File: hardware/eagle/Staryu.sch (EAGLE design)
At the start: 29 parts, among them IC1 ATMEGA32U2-TQFP, SW1 CHERRY-MX-LED, SW2 CHERRY-MX-LED, SW3 CHERRY-MX-LED, SW4 CHERRY-MX-LED, SW5 CHERRY-MX-LED, Y1 16MHZ

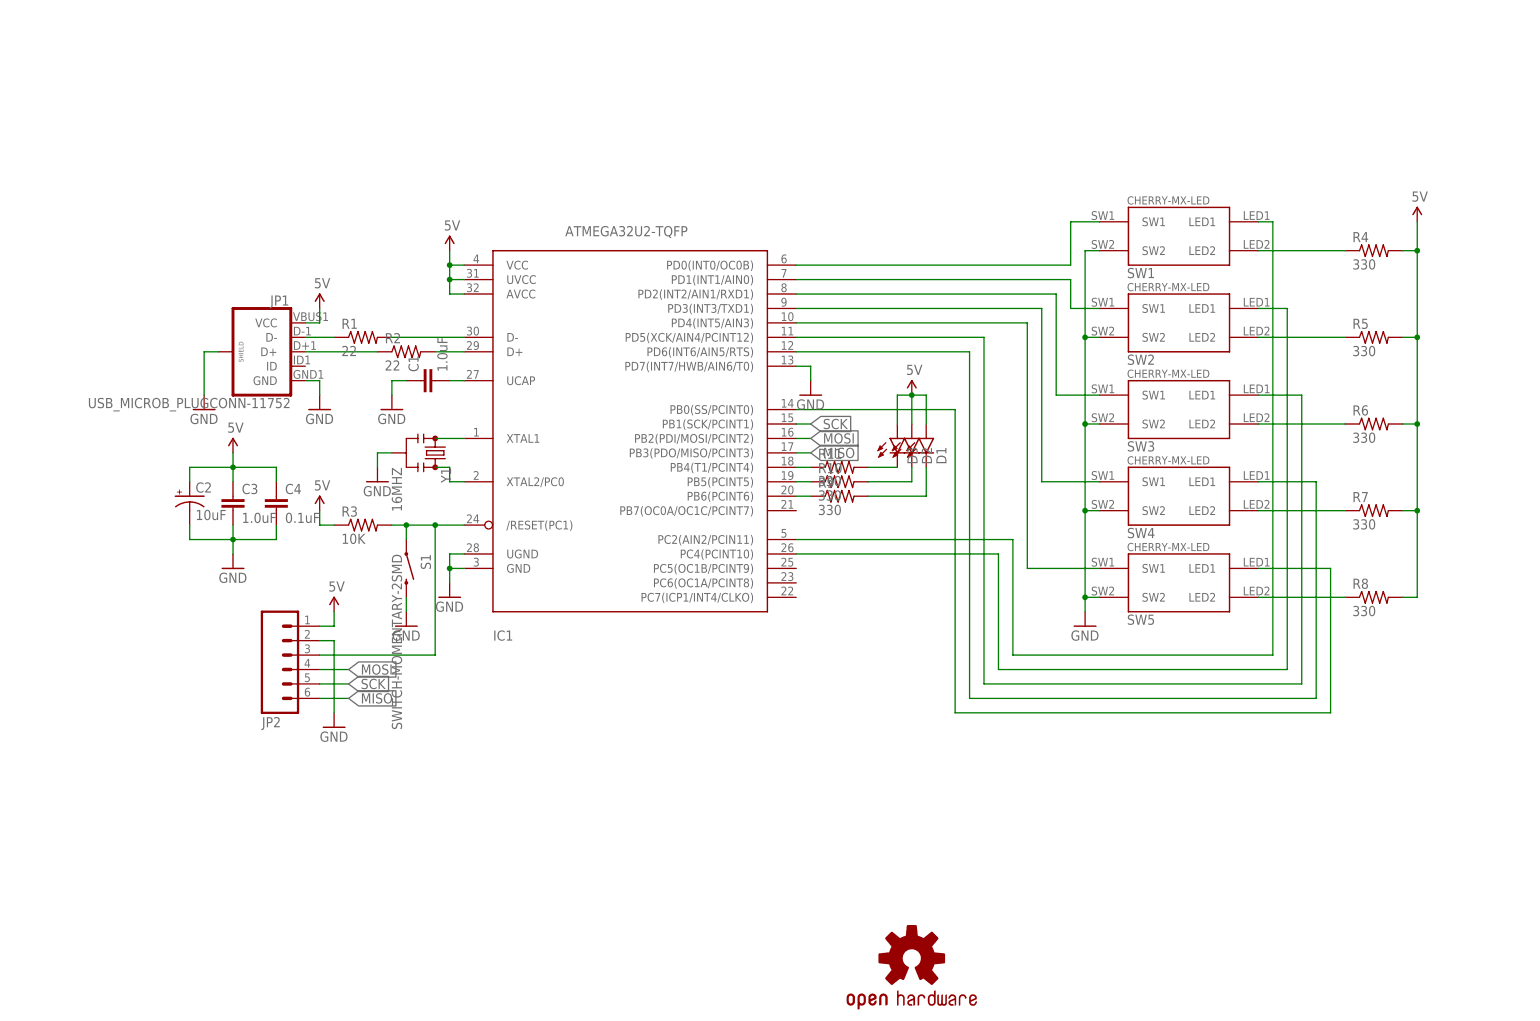
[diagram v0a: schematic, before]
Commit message: Update eagle files and schematics to v1.2 - Change 3 LEDs on top side to WS2812B
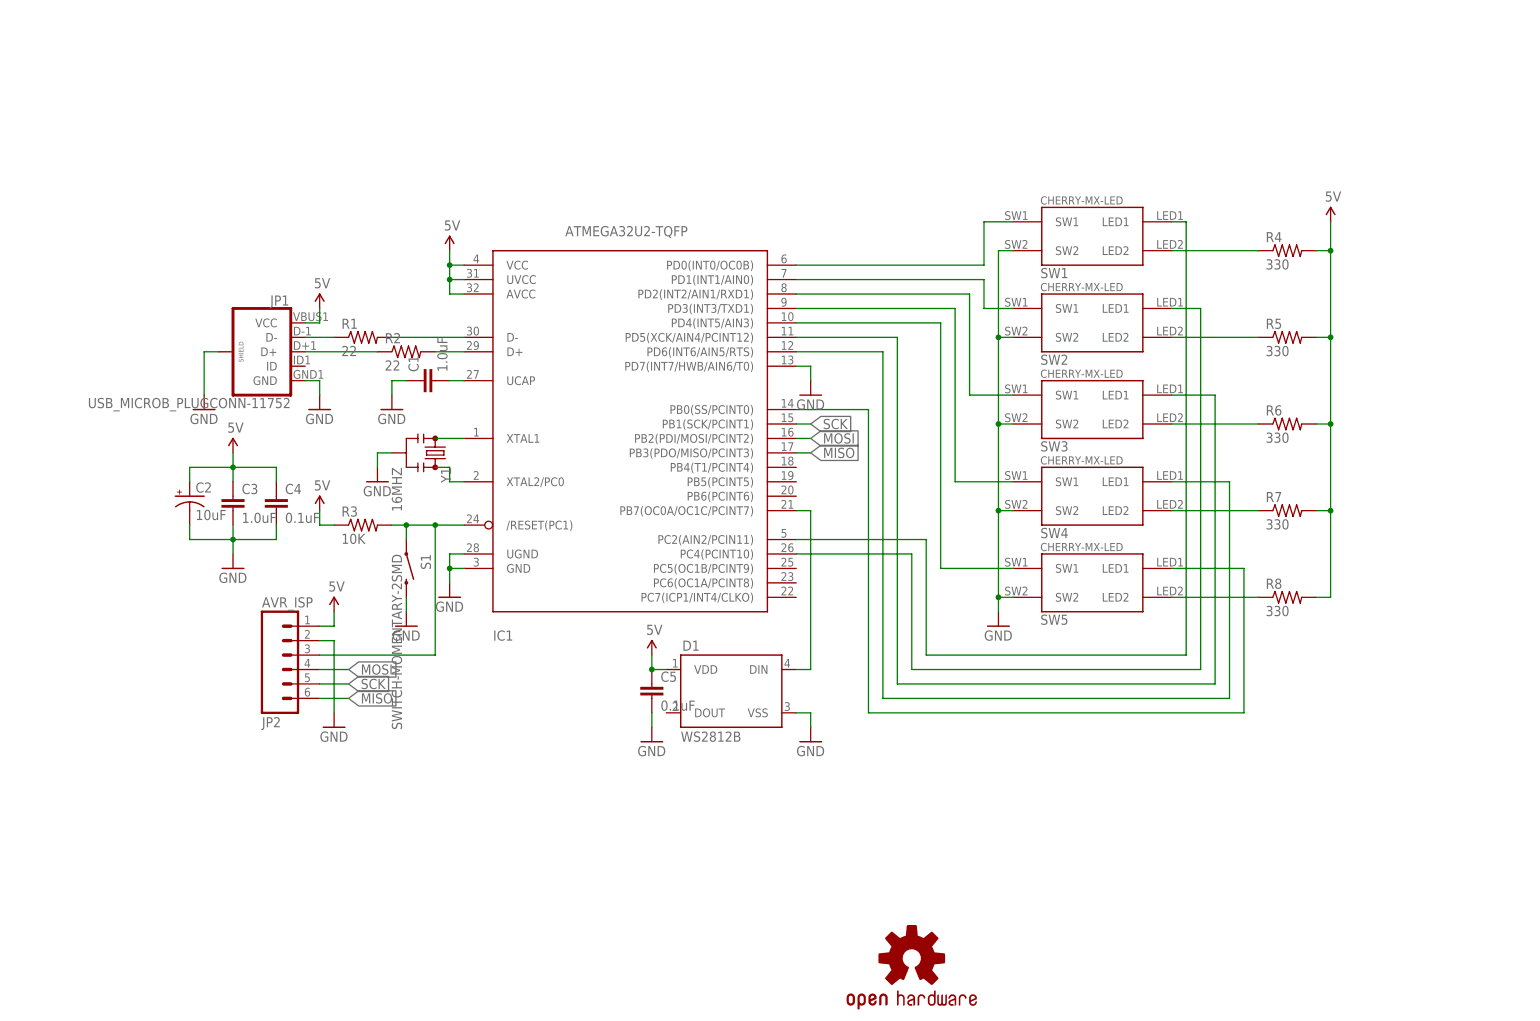
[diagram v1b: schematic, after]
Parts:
- removed D2, D3: (no value), SparkFun-LED:LED1206
- removed R10, R11, R9: 330, SparkFun-Resistors:330OHM1/10W1%(0603)
- added C5: 0.1uF, SparkFun-Capacitors:0.1UF-25V(+80/-20%)(0603)
- D1: value (none) -> WS2812B; device SparkFun-LED:LED1206 -> SparkFun-LED:WS2812B
- JP2: value (none) -> AVR_ISP
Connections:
- removed net N$20: IC1.PB5(PCINT5), R10.1
- removed net N$21: IC1.PB6(PCINT6), R9.1
- removed net N$27: D3.C, R11.2
- removed net N$28: D2.C, R10.2
- removed net N$29: D1.C, R9.2
- net 5V: now also C5.1, D1.VDD; no longer D1.A, D2.A, D3.A
- net GND: now also C5.2, D1.VSS
- net N$19: now also D1.DIN, IC1.PB7(OC0A/OC1C/PCINT7); no longer IC1.PB4(T1/PCINT4), R11.1
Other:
- moved on the sheet: R4, R5, R6, R7, R8, SW1, SW2, SW3, SW4, SW5

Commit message: Update eagle files and schematics to v1.2 - Compact outline - Relocate LED and re-route circuits - Add logos
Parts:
- added LOGO2: NOUKENSHA-LOGOM, Noukensha:NOUKENSHA-LOGOM
- added LOGO3: OSHW-LOGOM, Noukensha:OSHW-LOGOM
- added U$3: CC-BY-SANIX, cc-by-sa:CC-BY-SANIX
- C1, C3: device SparkFun-Capacitors:1.0UF-16V-10%(0603) -> SparkFun-Capacitors:CAP0805
- C4, C5: device SparkFun-Capacitors:0.1UF-25V(+80/-20%)(0603) -> SparkFun-Capacitors:CAP0805
- D1: device SparkFun-LED:WS2812B -> ws2812:WS2812BNOSILK
- LOGO1: value OSHW-LOGOM -> STARYU-LOGO; device SparkFun-Aesthetics:OSHW-LOGOM -> Noukensha:STARYU-LOGO
- R1, R2: device SparkFun-Resistors:22OHM1/10W1%(0603) -> SparkFun-Resistors:RESISTOR0805-RES
- R3: device SparkFun-Resistors:10KOHM-1/10W-1%(0603)0603 -> SparkFun-Resistors:RESISTOR0805-RES
- R4, R5, R6, R7, R8: device SparkFun-Resistors:330OHM1/10W1%(0603) -> SparkFun-Resistors:RESISTOR0805-RES
- renumbered IC1 to U1
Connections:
- new net SHIELD: JP1.SHIELD
- net GND: now also S1.1; no longer JP1.SHIELD, S1.2
- net N$19: now also U1.PC6(OC1A/PCINT8); no longer U1.PB7(OC0A/OC1C/PCINT7)
- net N$31: now also U1.PC7(ICP1/INT4/CLKO); no longer U1.PC4(PCINT10)
- net N$8: now also S1.2; no longer S1.1
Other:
- moved on the sheet: S1

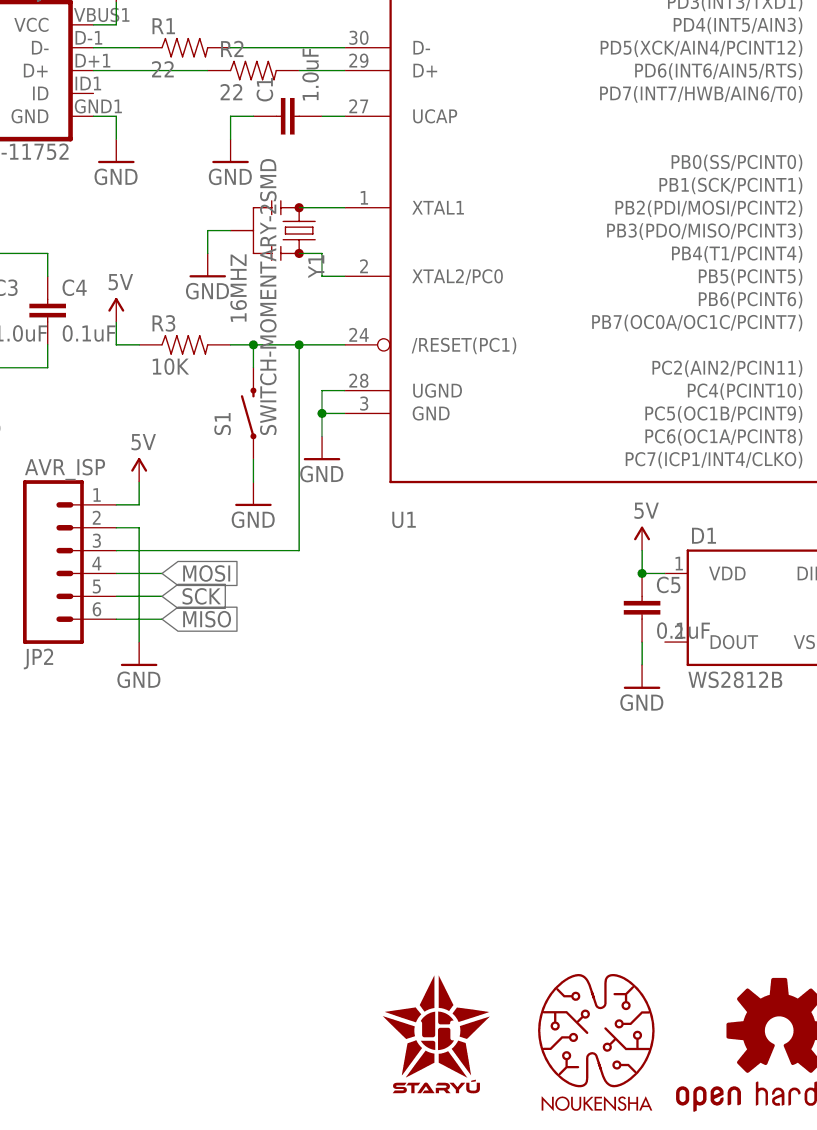
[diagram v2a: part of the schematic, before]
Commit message: Update eagle files and schematics to v1.3 - Contract outline even more - Change logo to exposing copper - Change footprint of resonator to be easier to solder
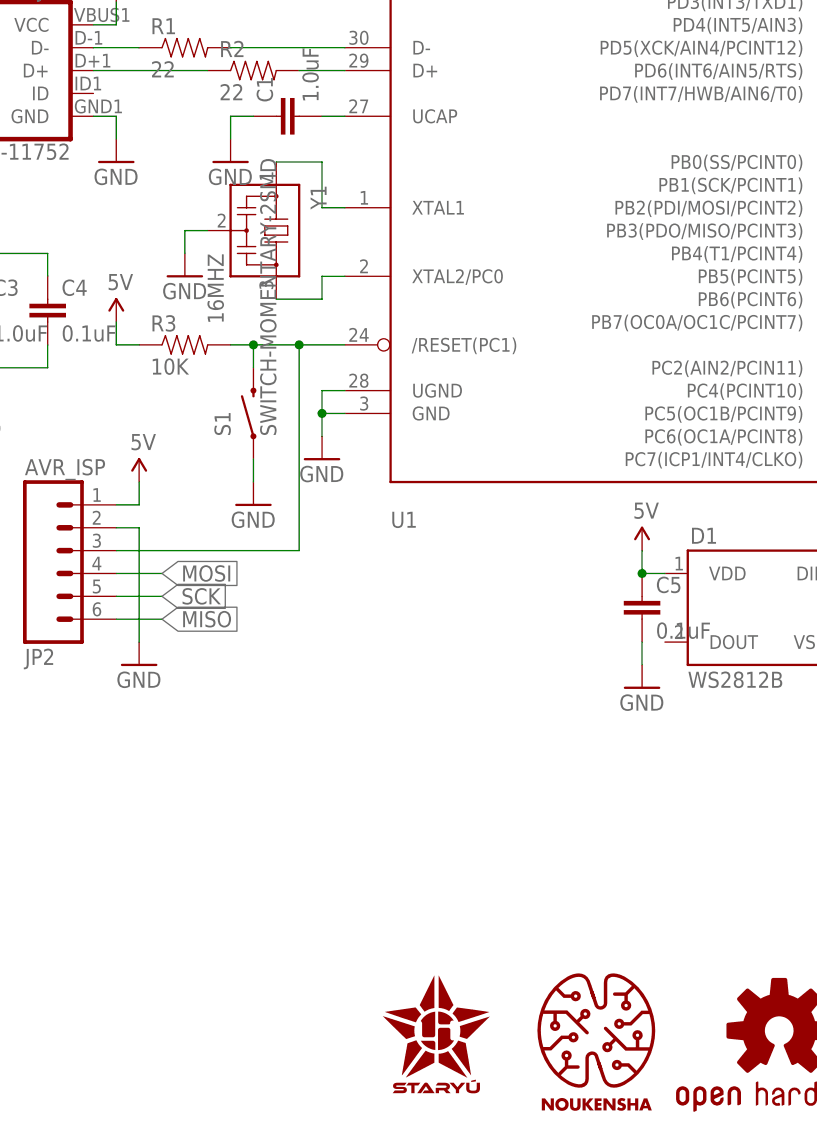
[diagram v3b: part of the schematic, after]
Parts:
- LOGO1: value STARYU-LOGO -> STARYU_LOGO; device Noukensha:STARYU-LOGO -> Noukensha:STARYU_LOGO
- LOGO2: value NOUKENSHA-LOGOM -> NOUKENSHA_LOGO.3_EXP; device Noukensha:NOUKENSHA-LOGOM -> Noukensha:NOUKENSHA_LOGO.3_EXP
- LOGO3: value OSHW-LOGOM -> OSHW_LOGOM_EXP; device Noukensha:OSHW-LOGOM -> Noukensha:OSHW_LOGOM_EXP
- Y1: device SparkFun-FreqCtrl:RESONATOR16MHZ -> cstce-resonator:CSTCR6M00G53Z
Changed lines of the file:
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@@
 <setting verticaltext="up"/>
 </settings>
-<grid distance="0.1" unitdist="inch" unit="mil" style="lines" multiple="1" display="no" altdistance="0.01" altunitdist="inch" altunit="mil"/>
+<grid distance="0.1" unitdist="inch" unit="inch" style="lines" multiple="1" display="no" altdistance="0.01" altunitdist="inch" altunit="inch"/>
 <layers>
 <layer number="1" name="Top" color="4" fill="1" visible="no" active="no"/>
@@
 <part name="FRAME1" library="SparkFun-Aesthetics" deviceset="FRAME-A4L" device="">
 <attribute name="CNAME" value="Noukensha"/>
-<attribute name="CREVISION" value="1.2"/>
+<attribute name="CREVISION" value="1.3"/>
 <attribute name="DESIGNER" value="Kai Ryu"/>
 </part>
@@
 <part name="GND1" library="SparkFun-Aesthetics" deviceset="GND" device=""/>
 <part name="SUPPLY2" library="SparkFun-Aesthetics" deviceset="5V" device=""/>
-<part name="Y1" library="SparkFun-FreqCtrl" deviceset="RESONATOR" device="16MHZ" value="16MHZ"/>
+<part name="Y1" library="cstce-resonator" deviceset="CSTCR" device="" technology="6M00G53Z" value="16MHZ"/>
 <part name="GND2" library="SparkFun-Aesthetics" deviceset="GND" device=""/>
 <part name="C1" library="SparkFun-Capacitors" deviceset="CAP" device="0805" value="1.0uF"/>
@@
 <part name="SUPPLY7" library="SparkFun-Aesthetics" deviceset="5V" device=""/>
 <part name="JP2" library="SparkFun-Connectors" deviceset="M06" device="NO_SILK_FEMALE_PTH" value="AVR_ISP"/>
-<part name="LOGO3" library="Noukensha" deviceset="OSHW-LOGO" device="M" value="OSHW-LOGOM"/>
+<part name="LOGO3" library="Noukensha" deviceset="OSHW_LOGO" device="M_EXP" value="OSHW_LOGOM_EXP"/>
 <part name="D1" library="ws2812" deviceset="WS2812B" device="NOSILK" value="WS2812B"/>
 <part name="GND11" library="SparkFun-Aesthetics" deviceset="GND" device=""/>
 <part name="GND12" library="SparkFun-Aesthetics" deviceset="GND" device=""/>
 <part name="C5" library="SparkFun-Capacitors" deviceset="CAP" device="0805" value="0.1uF"/>
-<part name="LOGO1" library="Noukensha" deviceset="STARYU-LOGO" device=""/>
-<part name="LOGO2" library="Noukensha" deviceset="NOUKENSHA-LOGO" device="M" value="NOUKENSHA-LOGOM"/>
+<part name="LOGO1" library="Noukensha" deviceset="STARYU_LOGO" device=""/>
 <part name="U$3" library="cc-by-sa" deviceset="CC-BY-SA" device="NIX" value="CC-BY-SANIX"/>
+<part name="LOGO2" library="Noukensha" deviceset="NOUKENSHA_LOGO" device=".3_EXP" value="NOUKENSHA_LOGO.3_EXP"/>
 </parts>
 <sheets>
@@
 <instance part="GND1" gate="1" x="60.96" y="111.76"/>
 <instance part="SUPPLY2" gate="G$1" x="83.82" y="139.7"/>
-<instance part="Y1" gate="G$1" x="81.28" y="104.14" rot="R270"/>
-<instance part="GND2" gate="1" x="71.12" y="99.06"/>
+<instance part="Y1" gate="G$1" x="78.74" y="104.14" rot="R270"/>
+<instance part="GND2" gate="1" x="68.58" y="99.06"/>
 <instance part="C1" gate="G$1" x="81.28" y="116.84" rot="R90"/>
 <instance part="GND3" gate="1" x="73.66" y="111.76"/>
@@
 <instance part="C5" gate="G$1" x="119.38" y="60.96"/>
 <instance part="LOGO1" gate="G$1" x="96.52" y="15.24"/>
+<instance part="U$3" gate="G$1" x="167.64" y="15.24"/>
 <instance part="LOGO2" gate="G$1" x="114.3" y="15.24"/>
-<instance part="U$3" gate="G$1" x="167.64" y="15.24"/>
 </instances>
 <busses>
@@
 <segment>
 <pinref part="GND2" gate="1" pin="GND"/>
-<wire x1="71.12" y1="101.6" x2="71.12" y2="104.14" width="0.1524" layer="91"/>
+<wire x1="68.58" y1="101.6" x2="68.58" y2="104.14" width="0.1524" layer="91"/>
 <pinref part="Y1" gate="G$1" pin="2"/>
-<wire x1="71.12" y1="104.14" x2="73.66" y2="104.14" width="0.1524" layer="91"/>
+<wire x1="68.58" y1="104.14" x2="71.12" y2="104.14" width="0.1524" layer="91"/>
 </segment>
 <segment>
@@
 <pinref part="Y1" gate="G$1" pin="1"/>
 <pinref part="U1" gate="G$1" pin="XTAL1"/>
-<wire x1="81.28" y1="106.68" x2="86.36" y2="106.68" width="0.1524" layer="91"/>
+<wire x1="78.74" y1="111.76" x2="83.82" y2="111.76" width="0.1524" layer="91"/>
+<wire x1="83.82" y1="111.76" x2="83.82" y2="106.68" width="0.1524" layer="91"/>
+<wire x1="83.82" y1="106.68" x2="86.36" y2="106.68" width="0.1524" layer="91"/>
 </segment>
 </net>
@@
 <segment>
 <pinref part="Y1" gate="G$1" pin="3"/>
-<wire x1="81.28" y1="101.6" x2="83.82" y2="101.6" width="0.1524" layer="91"/>
-<wire x1="83.82" y1="101.6" x2="83.82" y2="99.06" width="0.1524" layer="91"/>
+<wire x1="78.74" y1="96.52" x2="83.82" y2="96.52" width="0.1524" layer="91"/>
+<wire x1="83.82" y1="96.52" x2="83.82" y2="99.06" width="0.1524" layer="91"/>
 <pinref part="U1" gate="G$1" pin="XTAL2/PC0"/>
 <wire x1="83.82" y1="99.06" x2="86.36" y2="99.06" width="0.1524" layer="91"/>
